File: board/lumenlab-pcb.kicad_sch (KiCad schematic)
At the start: 32 parts, among them J1 2.1mm Barrel Jack, J2 Conn_01x04_Pin, SW1 SW_SPST, U1 MP2338, U2 AP7361C-33E, U3 ESP32-WROOM-32D, U4 SN74AHC1G125DCKR, U5 SN74HC14N

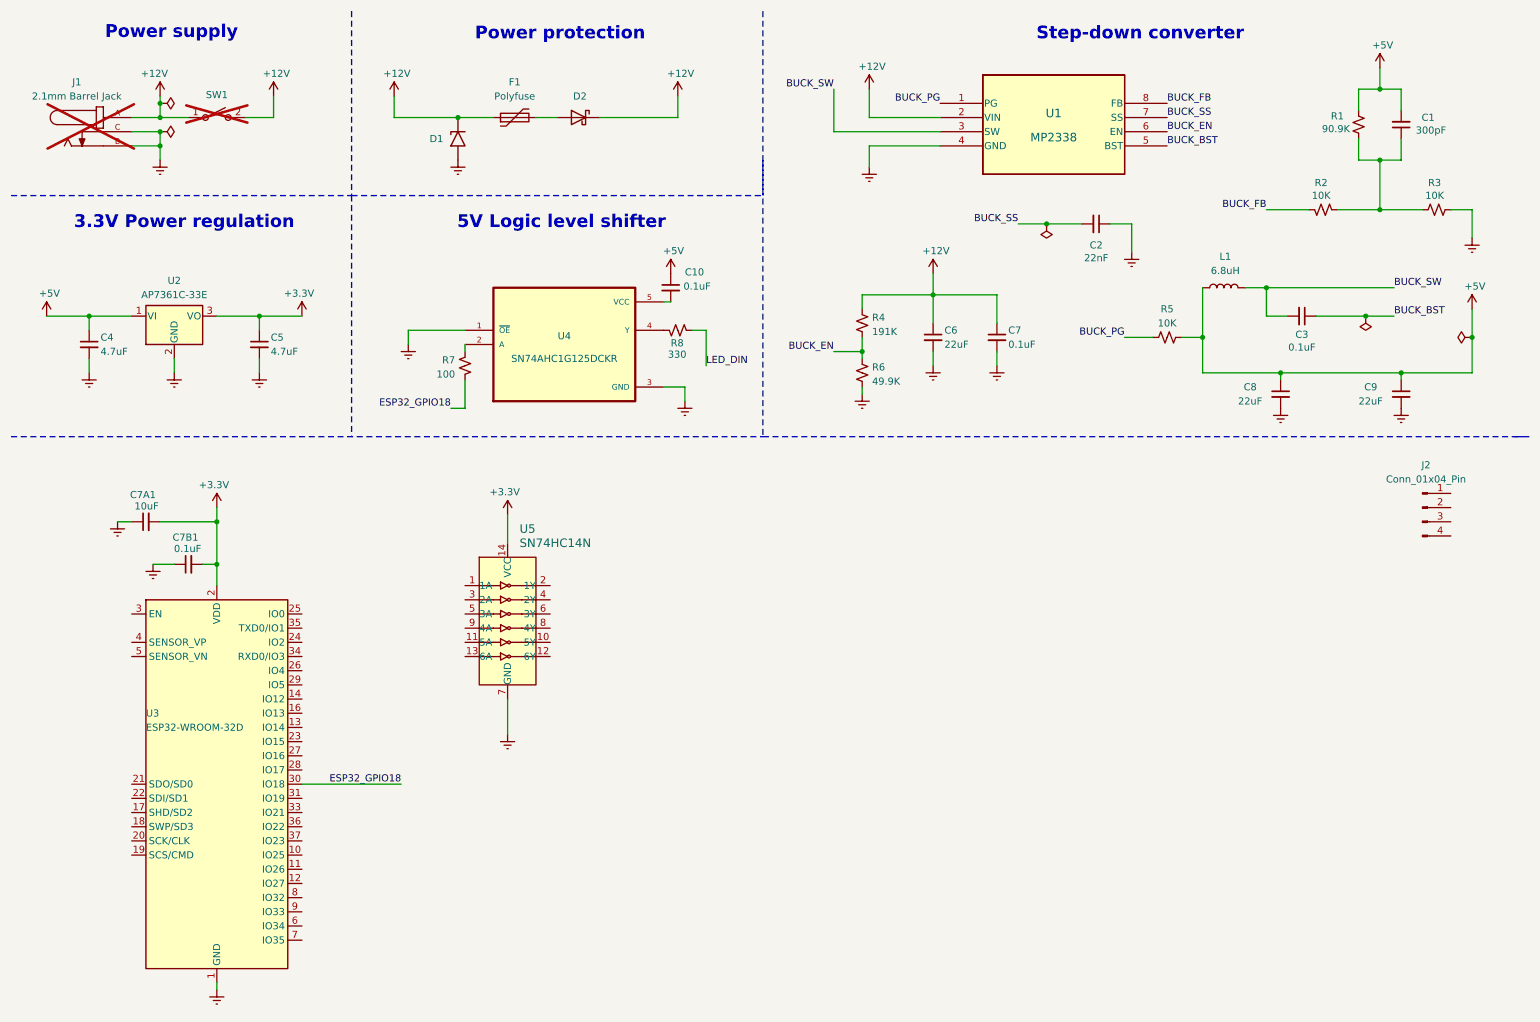
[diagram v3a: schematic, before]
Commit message: Add linear taper potentiometer for brightness control
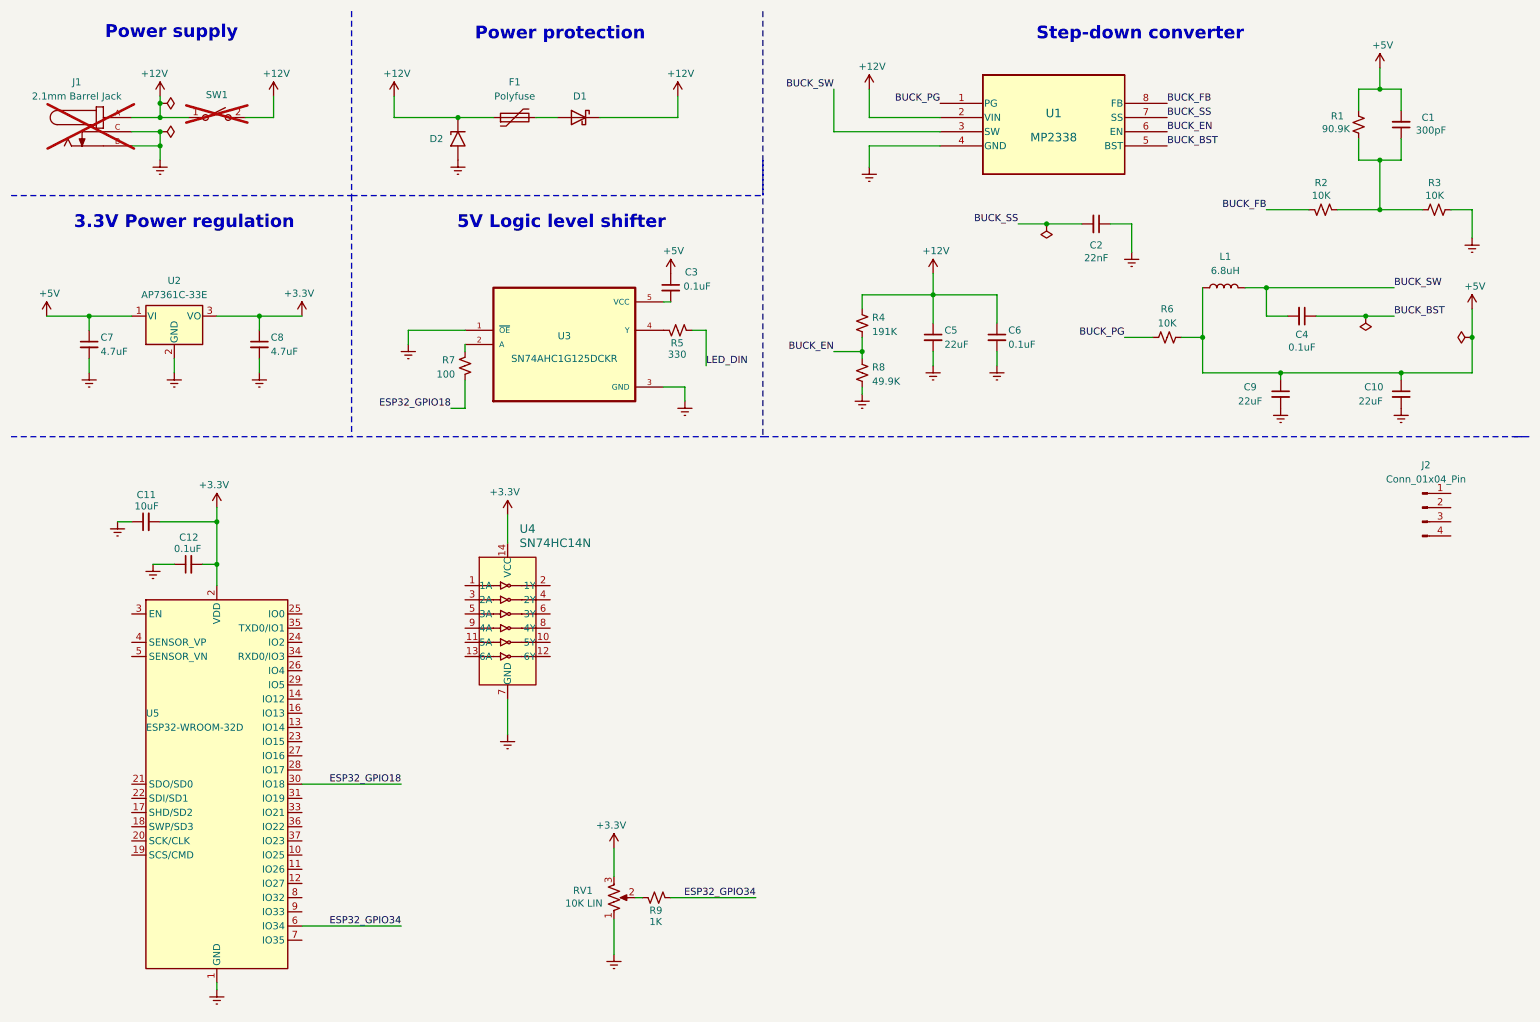
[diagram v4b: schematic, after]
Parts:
- added R9: 1K, Resistor_SMD:R_0603_1608Metric_Pad0.98x0.95mm_HandSolder, symbol Device:R_Small_US
- added RV1: 10K LIN, Potentiometer_THT:Potentiometer_Piher_T-16L_Single_Vertical_Hole, symbol Device:R_Potentiometer_US
- renumbered C9 to C10, C7A1 to C11, C7B1 to C12, C10 to C3, C3 to C4, C6 to C5, C7 to C6, C4 to C7, C5 to C8, C8 to C9, D2 to D1, D1 to D2, R8 to R5, R5 to R6, R6 to R8, U4 to U3, U5 to U4, U3 to U5
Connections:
- net +3.3V: now also RV1.3
- net GND: now also RV1.1
- net ESP32_GPIO34: now reaches U5.6 (IO34)
- net ESP32_GPIO34: now also R9.1
- new net: R9.2, RV1.2

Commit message: Add potentiometers for LED brightness and audio volume
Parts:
- added RV2: 10K LOG, Potentiometer_THT:Potentiometer_Piher_T-16L_Single_Vertical_Hole, symbol Device:R_Potentiometer_US
- added U6: LM386MX, digikey-footprints:SOIC-8_W3.9mm, symbol dk_Linear-Amplifiers-Audio:LM386MX-1_NOPB
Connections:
- net +3.3V: now also RV2.3
- net GND: now also RV2.1
- new net AMP_IN: RV2.2, U6.3
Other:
- note added: "LED brightness control"
- note added: "Volume control"
- moved on the sheet: J2, R9, RV1

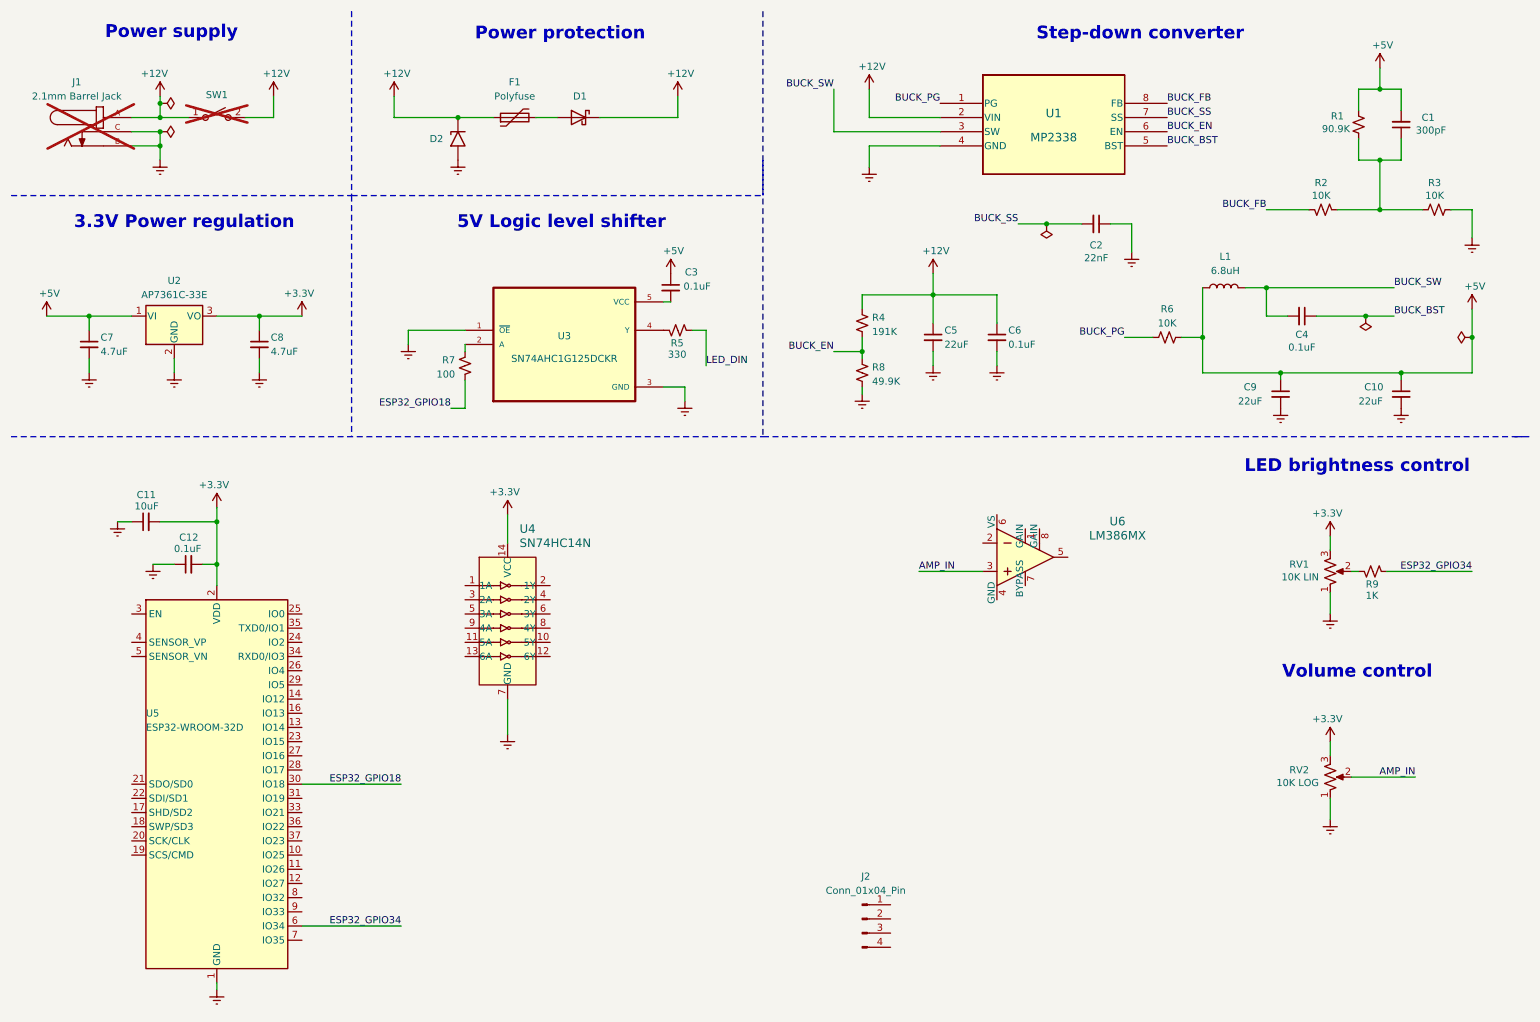
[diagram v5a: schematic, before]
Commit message: Add screw terminal and adjust formatting
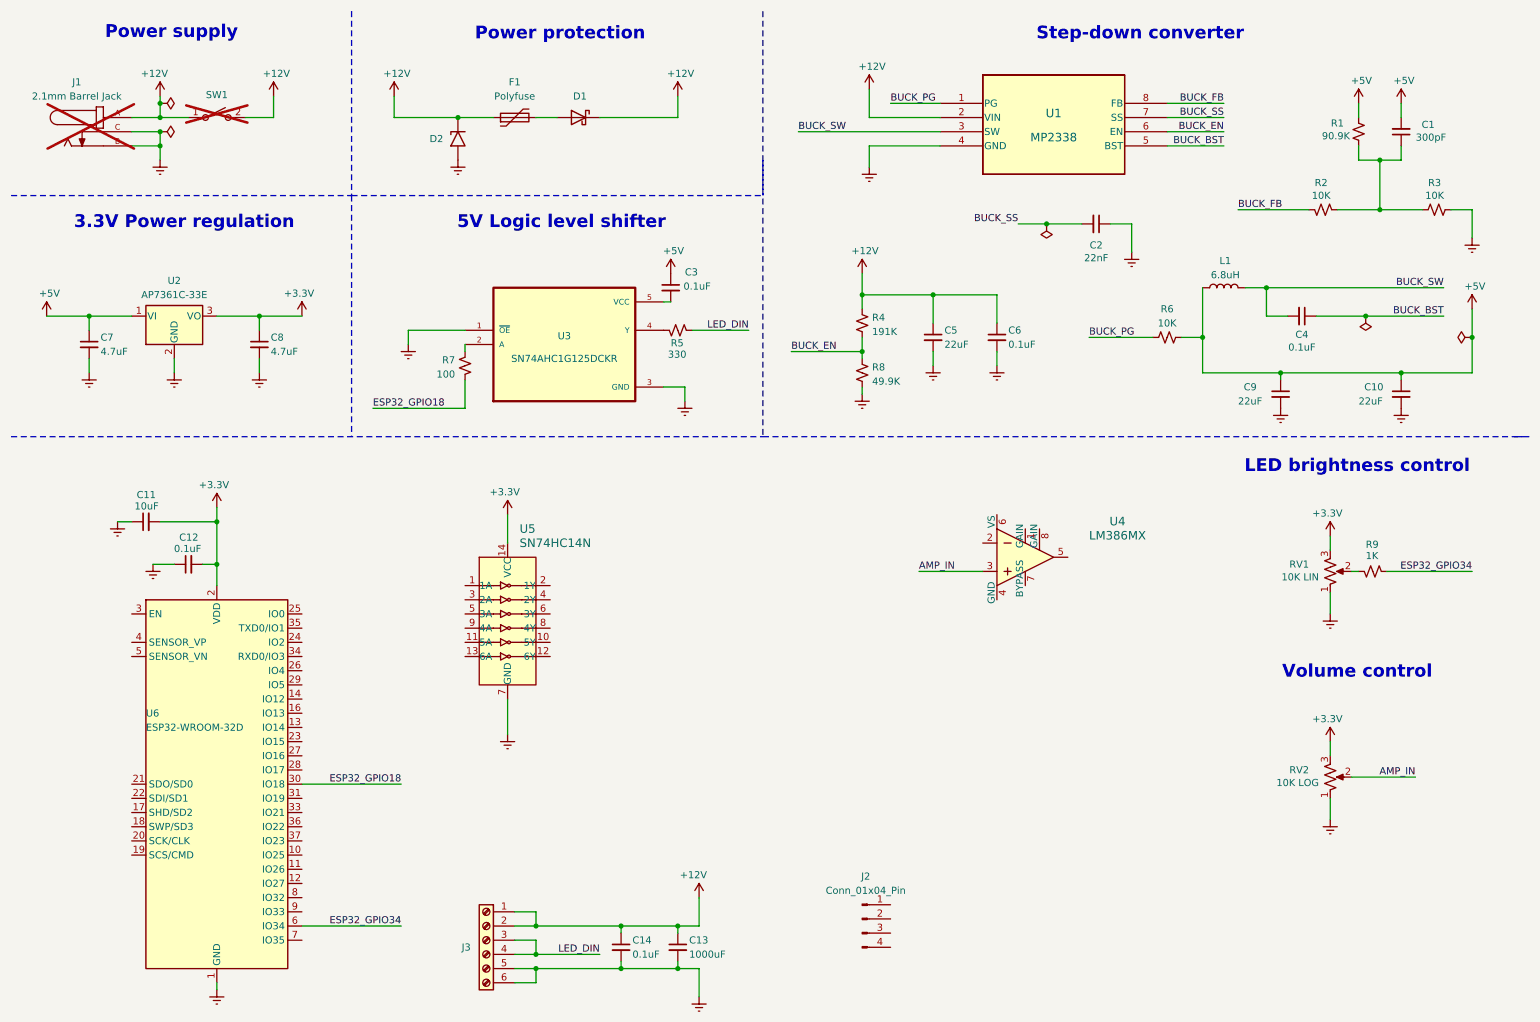
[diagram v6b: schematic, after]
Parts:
- added C13: 1000uF, Capacitor_THT:C_Radial_D10.0mm_H20.0mm_P5.00mm, symbol Device:C_Small
- added C14: 0.1uF, Capacitor_SMD:C_0603_1608Metric_Pad1.08x0.95mm_HandSolder, symbol Device:C_Small
- added J3: Screw_Terminal_01x06, TerminalBlock_Phoenix:TerminalBlock_Phoenix_PT-1,5-6-3.5-H_1x06_P3.50mm_Horizontal, symbol Connector:Screw_Terminal_01x06
- renumbered U6 to U4, U4 to U5, U5 to U6
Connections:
- net +12V: now also C13.1, C14.1, J3.1 (Pin_1), J3.2 (Pin_2)
- net GND: now also C13.2, C14.2, J3.5 (Pin_5), J3.6 (Pin_6)
- net LED_DIN: now also J3.3 (Pin_3), J3.4 (Pin_4)
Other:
- moved on the sheet: C1, R1
